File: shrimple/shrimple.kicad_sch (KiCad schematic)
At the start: 114 parts, among them U3 Pro Micro RP2040

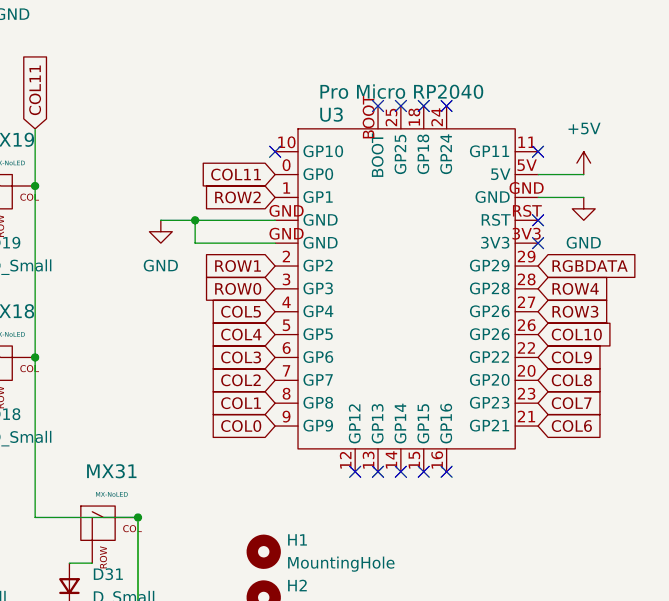
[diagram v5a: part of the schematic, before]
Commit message: flipped mcu and rerouted
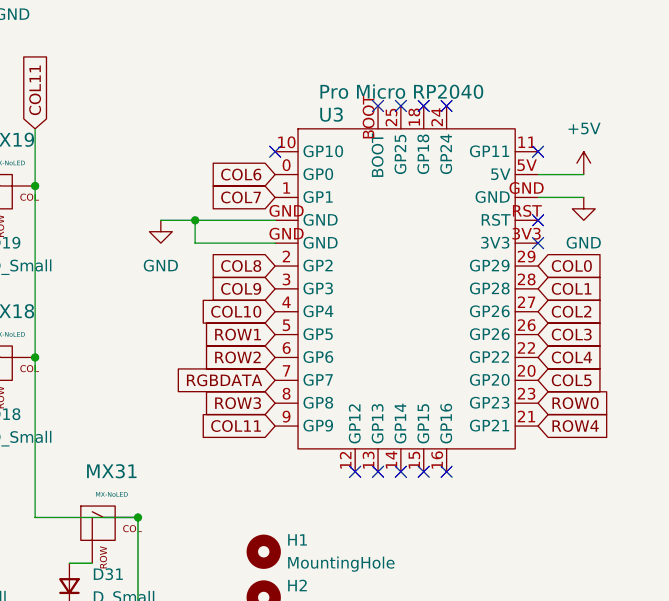
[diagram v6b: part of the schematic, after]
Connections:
- net COL0: now also U3.29 (GP29); no longer U3.9 (GP9)
- net COL1: now also U3.28 (GP28); no longer U3.8 (GP8)
- net COL10: now also U3.4 (GP4); no longer U3.26 (GP26)
- net COL11: now also U3.9 (GP9); no longer U3.0 (GP0)
- net COL2: now also U3.27 (GP26); no longer U3.7 (GP7)
- net COL3: now also U3.26 (GP26); no longer U3.6 (GP6)
- net COL4: now also U3.22 (GP22); no longer U3.5 (GP5)
- net COL5: now also U3.20 (GP20); no longer U3.4 (GP4)
- net COL6: now also U3.0 (GP0); no longer U3.21 (GP21)
- net COL7: now also U3.1 (GP1); no longer U3.23 (GP23)
- net COL8: now also U3.2 (GP2); no longer U3.20 (GP20)
- net COL9: now also U3.3 (GP3); no longer U3.22 (GP22)
- net RGBDATA: now also U3.7 (GP7); no longer U3.29 (GP29)
- net ROW0: now also U3.23 (GP23); no longer U3.3 (GP3)
- net ROW1: now also U3.5 (GP5); no longer U3.2 (GP2)
- net ROW2: now also U3.6 (GP6); no longer U3.1 (GP1)
- net ROW3: now also U3.8 (GP8); no longer U3.27 (GP26)
- net ROW4: now also U3.21 (GP21); no longer U3.28 (GP28)

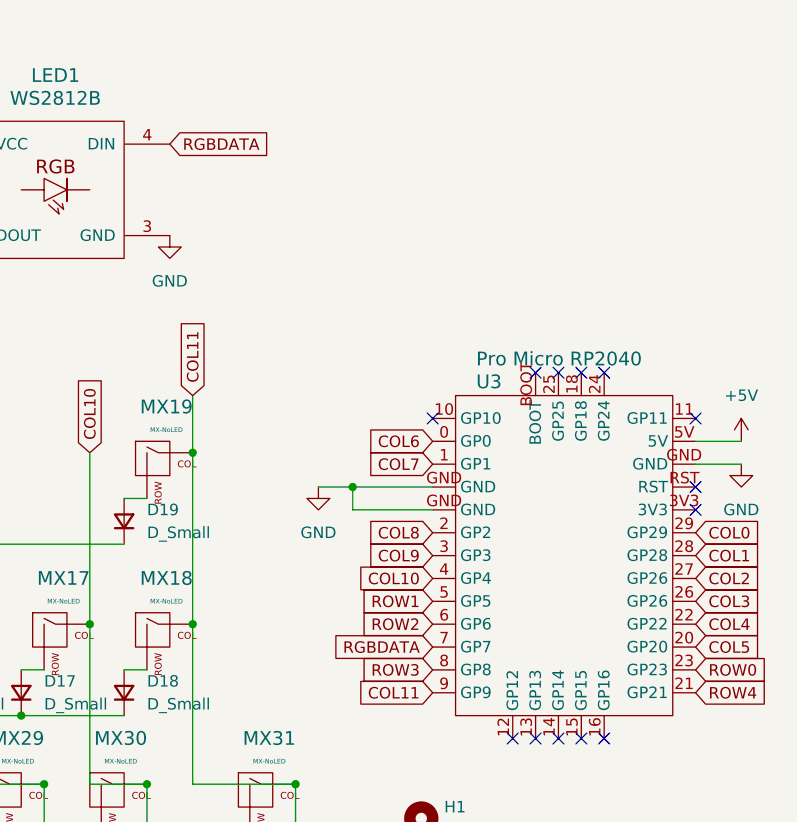
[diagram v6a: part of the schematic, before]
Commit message: added level shifter
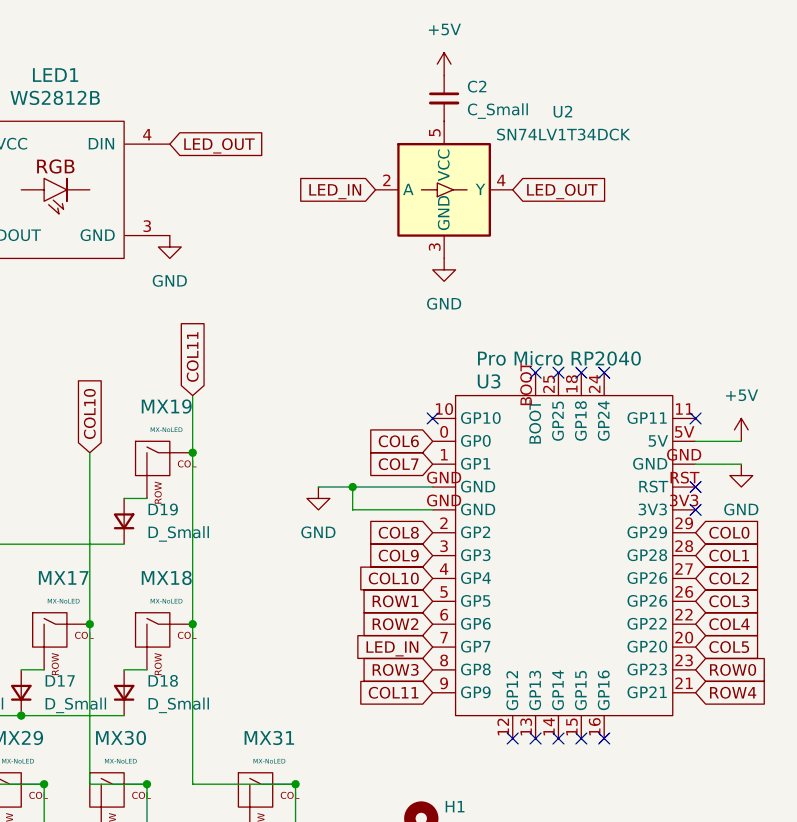
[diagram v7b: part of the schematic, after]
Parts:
- added C2: C_Small, Capacitor_SMD:C_0603_1608Metric_Pad1.08x0.95mm_HandSolder, symbol Device:C_Small
- added U2: SN74LV1T34DCK, Package_TO_SOT_SMD:SOT-353_SC-70-5, symbol Logic_LevelTranslator:SN74LV1T34DCK
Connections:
- net +5V: now also C2.1
- net GND: now also U2.3 (GND)
- net RGBDATA renamed LED_IN
- net LED_IN: now also U2.2 (A); no longer LED1.4 (DIN)
- new net: C2.2, U2.5 (VCC)
- new net LED_OUT: LED1.4 (DIN), U2.4 (Y)

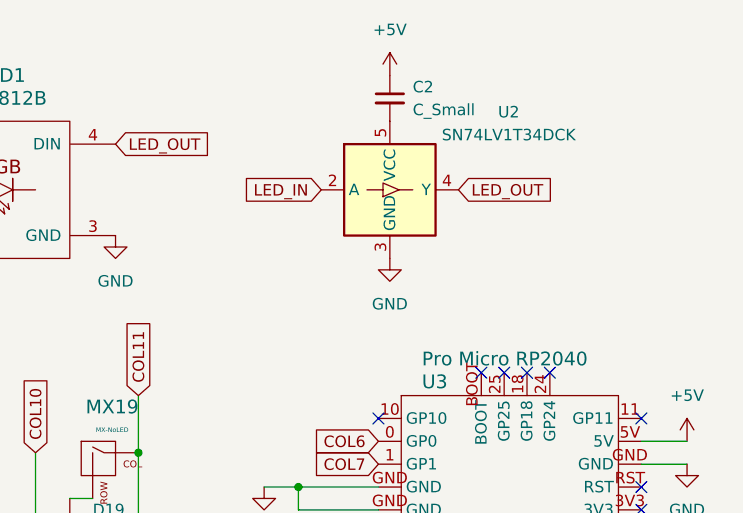
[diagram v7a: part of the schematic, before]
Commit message: fixed layout, added level shifter, made gerbers
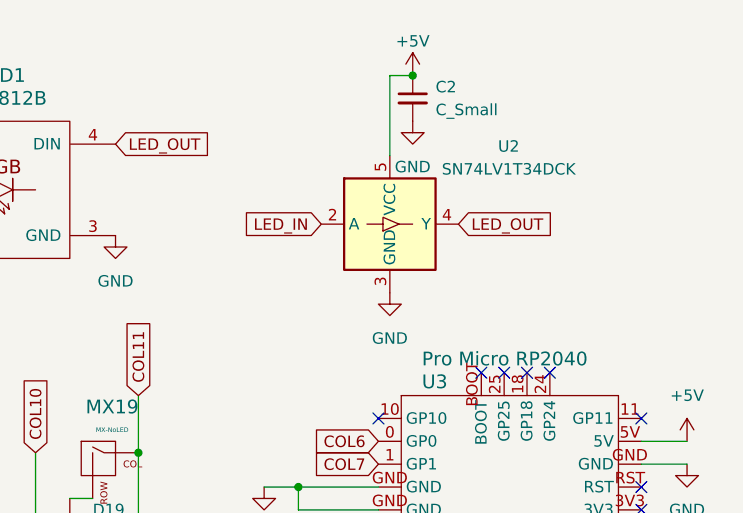
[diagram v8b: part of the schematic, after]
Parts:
- MX1, MX10, MX11, MX12, MX13, MX14, MX15, MX16, MX17, MX18, MX19, MX2, MX21, MX22, MX23, MX24, MX25, MX26, MX27, MX28, MX29, MX3, MX30, MX33, MX34, MX35, MX36, MX37, MX38, MX39, MX4, MX40, MX41, MX43, MX45, MX49, MX5, MX50, MX51, MX52, MX6, MX7, MX8, MX9: footprint hybrids:MX-1U-NoLED -> MX_V2:MX-Solderable-1U
- MX20: footprint hybrids:MX-1.5U-NoLED -> MX_V2:MX-Solderable-1.25U
- MX31: footprint hybrids:MX-1.5U-NoLED -> MX_V2:MX-Solderable-1.75U
- MX32: footprint hybrids:MX-1.75U-NoLED -> MX_V2:MX-Solderable-1.75U
- MX42, MX44, MX46: footprint hybrids:MX-1.25U-NoLED -> MX_V2:MX-Solderable-1.25U
- MX47: footprint hybrids:MX-2.25U-ReversedStabilizers-NoLED -> MX_V2:MX-Solderable-2.25U-ReversedStabilizers
- MX48: footprint hybrids:MX-2.75U-ReversedStabilizers-NoLED -> MX_V2:MX-Solderable-2.75U-ReversedStabilizers
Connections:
- net +5V: now also U2.5 (VCC)
- net GND: now also C2.2
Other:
- moved on the sheet: C2, U2
